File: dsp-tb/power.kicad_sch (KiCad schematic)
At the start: 16 parts, among them J1 Conn_01x03, U2 TLV76733QWDRBxQ1

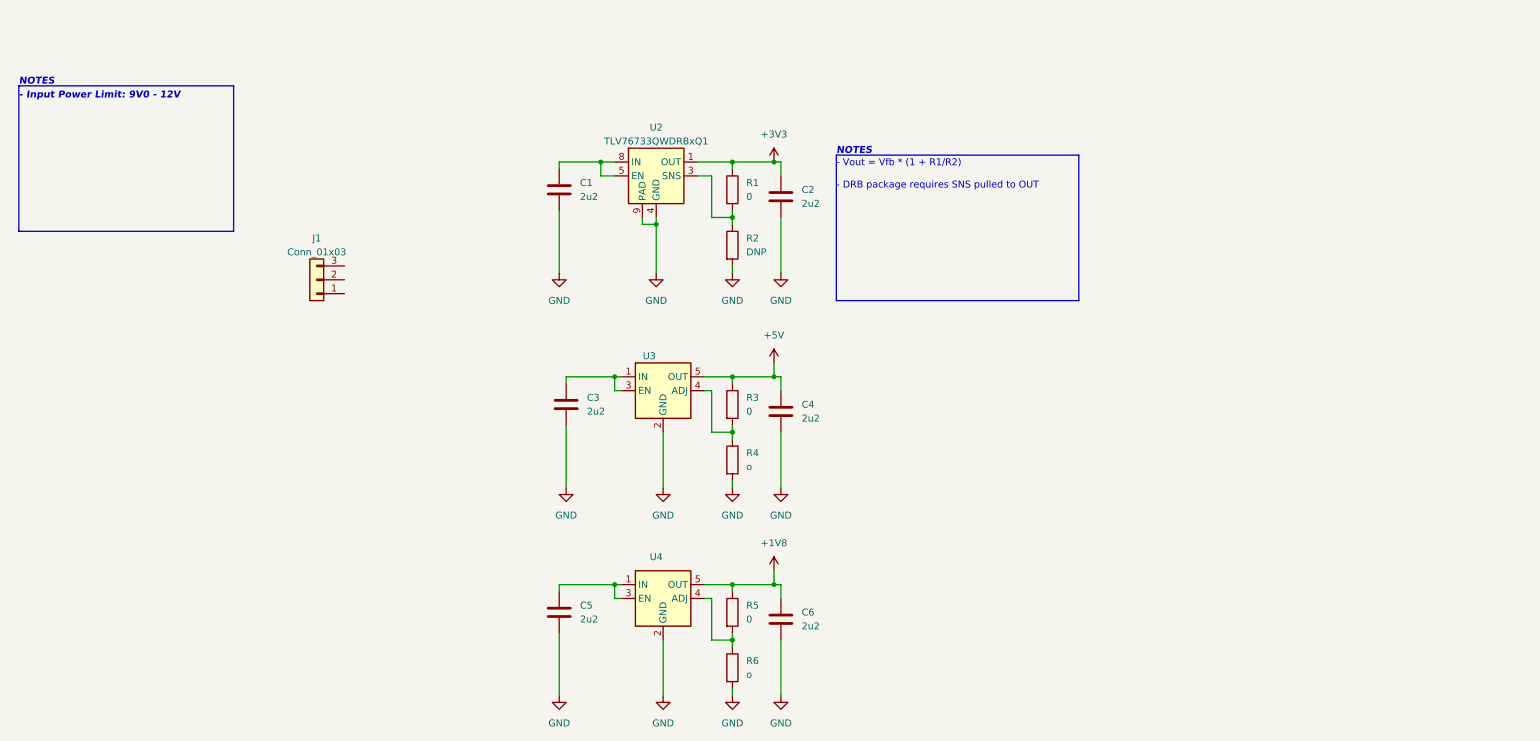
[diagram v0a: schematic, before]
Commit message: dsp-tb: start to include external components for mcu
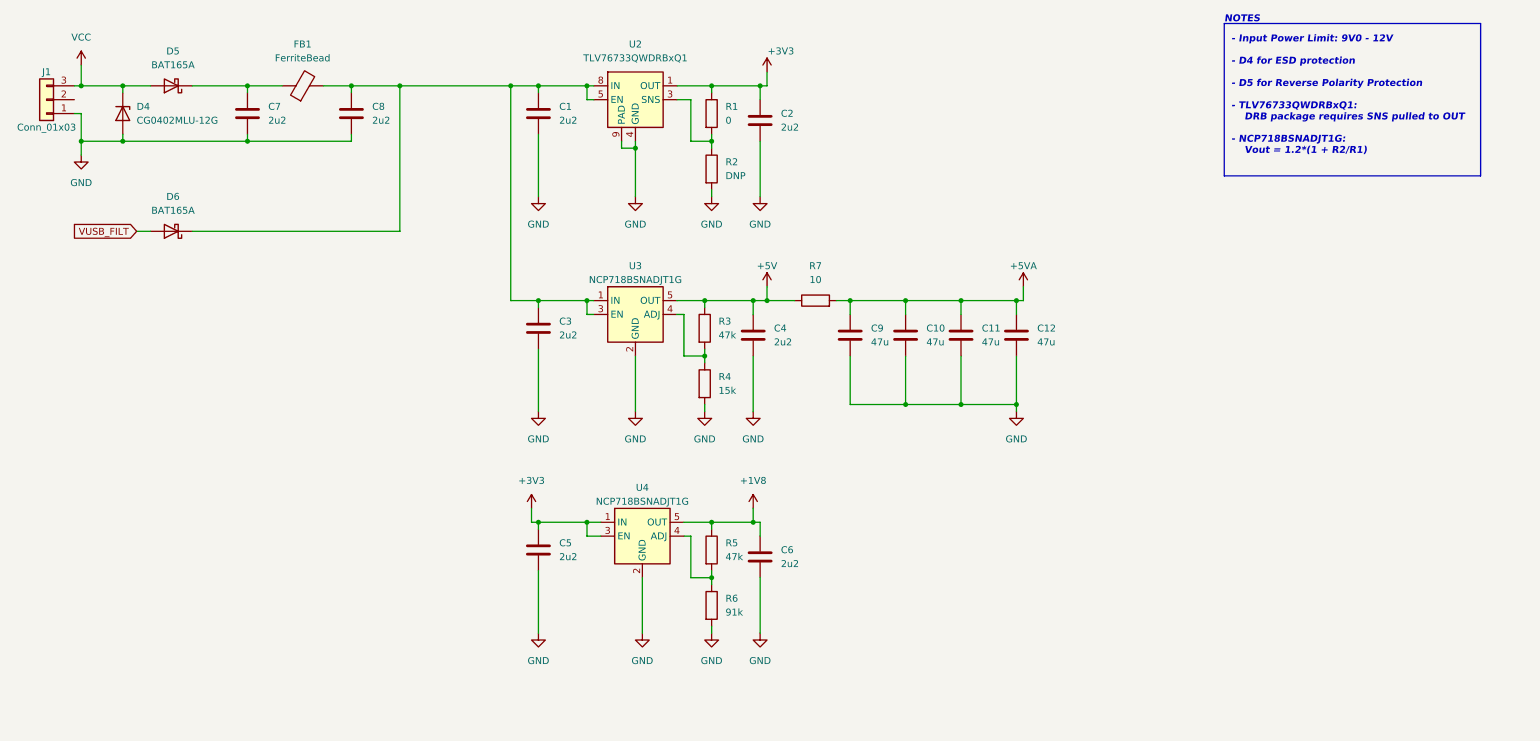
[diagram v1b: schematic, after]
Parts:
- added C10, C11, C12, C9: 47u, Capacitor_SMD:C_0402_1005Metric, symbol Device:C
- added C7, C8: 2u2, Capacitor_SMD:C_0402_1005Metric, symbol Device:C
- added D4: CG0402MLU-12G, Diode_SMD:D_0402_1005Metric, symbol Device:D_Zener
- added D5, D6: BAT165A, Diode_SMD:D_SOD-323_HandSoldering, symbol Device:D_Schottky
- added FB1: FerriteBead, Inductor_SMD:L_0402_1005Metric, symbol Device:FerriteBead
- added R7: 10, Resistor_SMD:R_0402_1005Metric, symbol Device:R
- J1: footprint (none) -> Connector_Molex:Molex_PicoBlade_53048-0310_1x03_P1.25mm_Horizontal
- R3, R5: value 0 -> 47k
- R4: value o -> 15k
- R6: value o -> 91k
- U3, U4: value ~ -> NCP718BSNADJT1G
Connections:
- net +3V3: now also C5.1, U4.1 (IN), U4.3 (EN)
- net +5V: now also R7.1
- net GND: now also J1.1 (Pin_1), C10.2, C11.2, C12.2, C7.2, C8.2, C9.2, D4.2 (A)
- net at C1.1, U2.5 (EN), U2.8 (IN): now also C3.1, U3.1 (IN), U3.3 (EN), C8.1, D6.1 (K), FB1.2
- net VCC: now reaches J1.3 (Pin_3)
- net VCC: now also D4.1 (K), D5.2 (A)
- new net: C7.1, D5.1 (K), FB1.1
- new net +5VA: C10.1, C11.1, C12.1, C9.1, R7.2
- new net VUSB_FILT: D6.2 (A)
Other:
- note added: "- Input Power Limit: 9V0 - 12V - D4 for ESD protection - D5 for Reverse Polarity Protection - TLV76733QWDRBxQ1: DRB package requires SNS pulled to OUT - NCP718BSNADJT1G: Vout = 1.2*(1 + R2/R1)"
- note removed: "- Input Power Limit: 9V0 - 12V"
- note removed: "- Vout = Vfb * (1 + R1/R2) - DRB package requires SNS pulled to OUT"
- moved on the sheet: C1, C2, C3, C4, C5, C6, J1, R1, R2, R3, R4, R5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

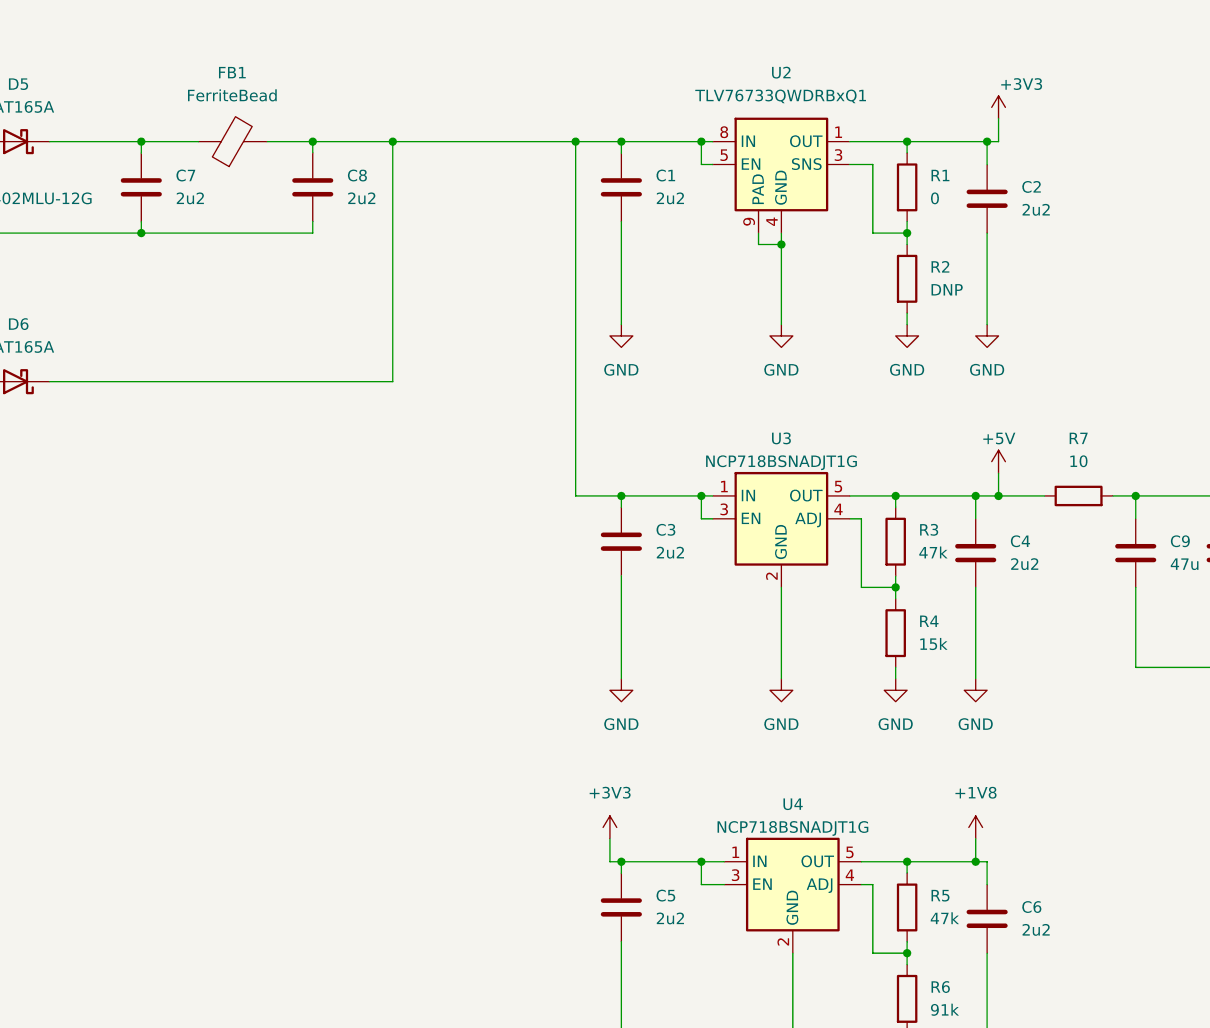
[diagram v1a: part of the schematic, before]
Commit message: dsp: boot0 and reset switches
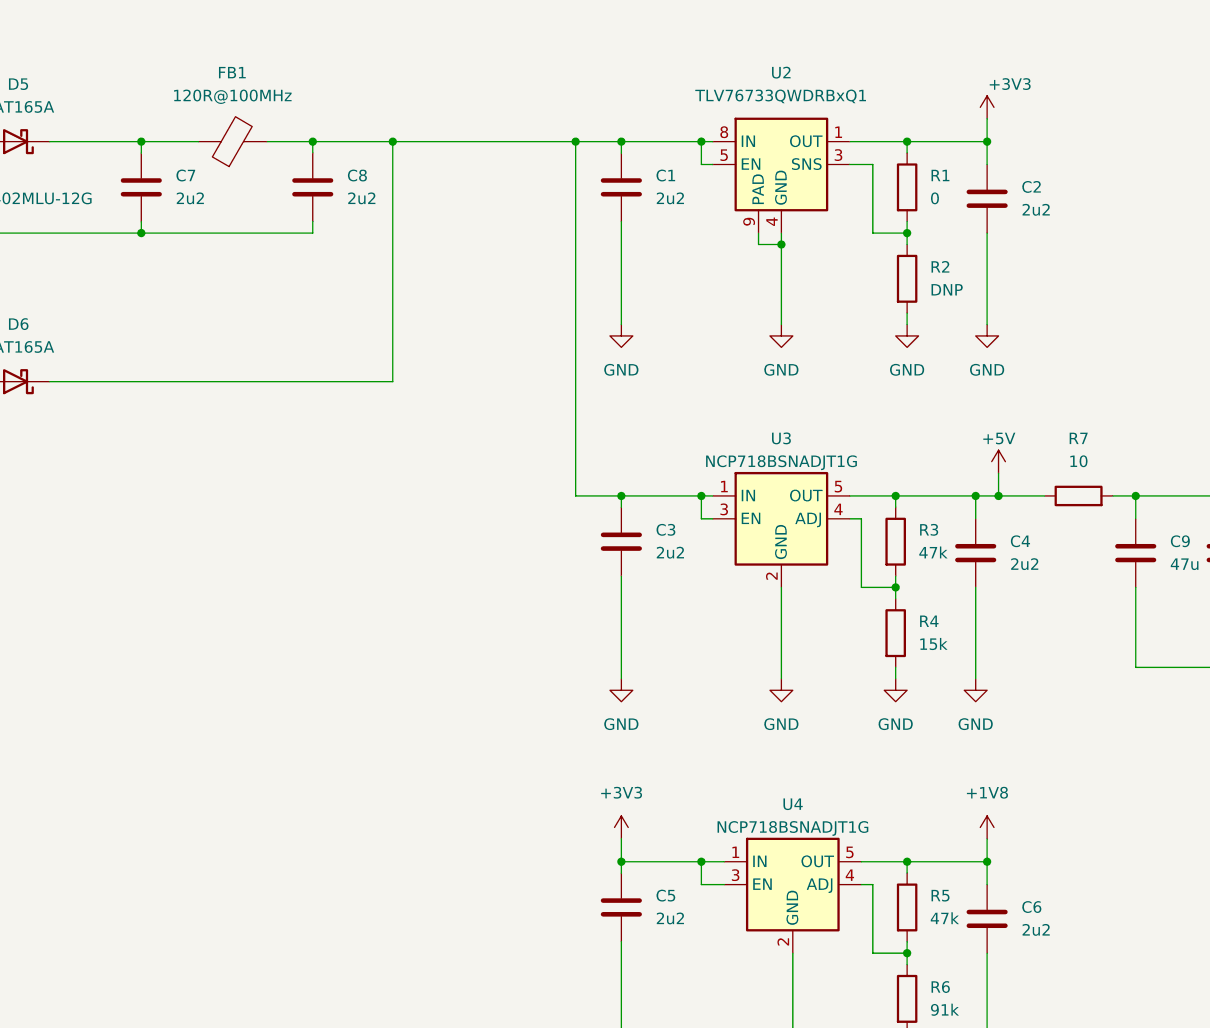
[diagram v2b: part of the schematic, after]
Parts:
- FB1: value FerriteBead -> 120R@100MHz
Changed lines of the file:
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@@
   (junction (at 142.24 36.83) (diameter 0) (color 0 0 0 0)
   )
-  (junction (at 149.86 106.68) (diameter 0) (color 0 0 0 0)
-  )
   (junction (at 142.24 26.67) (diameter 0) (color 0 0 0 0)
   )
@@
   (junction (at 119.38 26.67) (diameter 0) (color 0 0 0 0)
   )
+  (junction (at 151.13 106.68) (diameter 0) (color 0 0 0 0)
+  )
   (wire (pts (xy 34.29 26.67) (xy 39.37 26.67))
     (stroke (width 0) (type default))
@@
     (stroke (width 0) (type default))
   )
-  (wire (pts (xy 149.86 106.68) (xy 151.13 106.68))
-    (stroke (width 0) (type default))
-  )
   (wire (pts (xy 151.13 36.83) (xy 151.13 46.99))
     (stroke (width 0) (type default))
@@
     (stroke (width 0) (type default))
   )
-  (wire (pts (xy 109.22 104.14) (xy 109.22 106.68))
+  (wire (pts (xy 110.49 104.14) (xy 110.49 106.68))
     (stroke (width 0) (type default))
   )
@@
     (stroke (width 0) (type default))
   )
-  (wire (pts (xy 142.24 106.68) (xy 149.86 106.68))
+  (wire (pts (xy 142.24 106.68) (xy 151.13 106.68))
     (stroke (width 0) (type default))
   )
@@
     (stroke (width 0) (type default))
   )
-  (wire (pts (xy 109.22 106.68) (xy 110.49 106.68))
-    (stroke (width 0) (type default))
-  )
   (wire (pts (xy 140.97 67.31) (xy 140.97 66.04))
     (stroke (width 0) (type default))
@@
     (stroke (width 0) (type default))
   )
-  (wire (pts (xy 152.4 26.67) (xy 151.13 26.67))
-    (stroke (width 0) (type default))
-  )
   (wire (pts (xy 57.15 26.67) (xy 63.5 26.67))
     (stroke (width 0) (type default))
@@
     (stroke (width 0) (type default))
   )
-  (wire (pts (xy 149.86 104.14) (xy 149.86 106.68))
+  (wire (pts (xy 151.13 104.14) (xy 151.13 106.68))
     (stroke (width 0) (type default))
   )
@@
     (stroke (width 0) (type default))
   )
-  (wire (pts (xy 152.4 24.13) (xy 152.4 26.67))
+  (wire (pts (xy 151.13 24.13) (xy 151.13 26.67))
     (stroke (width 0) (type default))
   )
@@
       (effects (font (size 1.27 1.27)))
     )
-    (property "Value" "FerriteBead" (at 67.2592 21.59 90)
+    (property "Value" "120R@100MHz" (at 67.2592 21.59 90)
       (effects (font (size 1.27 1.27)))
     )
@@
     )
   )
-  (symbol (lib_id "power:+3V3") (at 109.22 104.14 0) (unit 1)
-    (in_bom yes) (on_board yes) (dnp no) (fields_autoplaced)
-    (property "Reference" "#PWR018" (at 109.22 107.95 0)
-      (effects (font (size 1.27 1.27)) hide)
-    )
-    (property "Value" "+3V3" (at 109.22 99.06 0)
-      (effects (font (size 1.27 1.27)))
-    )
-    (property "Footprint" "" (at 109.22 104.14 0)
-      (effects (font (size 1.27 1.27)) hide)
-    )
-    (property "Datasheet" "" (at 109.22 104.14 0)
+  (symbol (lib_id "power:+3V3") (at 110.49 104.14 0) (unit 1)
+    (in_bom yes) (on_board yes) (dnp no) (fields_autoplaced)
+    (property "Reference" "#PWR018" (at 110.49 107.95 0)
+      (effects (font (size 1.27 1.27)) hide)
+    )
+    (property "Value" "+3V3" (at 110.49 99.06 0)
+      (effects (font (size 1.27 1.27)))
+    )
+    (property "Footprint" "" (at 110.49 104.14 0)
+      (effects (font (size 1.27 1.27)) hide)
+    )
+    (property "Datasheet" "" (at 110.49 104.14 0)
       (effects (font (size 1.27 1.27)) hide)
     )
@@
     )
   )
-  (symbol (lib_id "power:+1V8") (at 149.86 104.14 0) (unit 1)
-    (in_bom yes) (on_board yes) (dnp no) (fields_autoplaced)
-    (property "Reference" "#PWR010" (at 149.86 107.95 0)
-      (effects (font (size 1.27 1.27)) hide)
-    )
-    (property "Value" "+1V8" (at 149.86 99.06 0)
-      (effects (font (size 1.27 1.27)))
-    )
-    (property "Footprint" "" (at 149.86 104.14 0)
-      (effects (font (size 1.27 1.27)) hide)
-    )
-    (property "Datasheet" "" (at 149.86 104.14 0)
+  (symbol (lib_id "power:+1V8") (at 151.13 104.14 0) (unit 1)
+    (in_bom yes) (on_board yes) (dnp no) (fields_autoplaced)
+    (property "Reference" "#PWR010" (at 151.13 107.95 0)
+      (effects (font (size 1.27 1.27)) hide)
+    )
+    (property "Value" "+1V8" (at 151.13 99.06 0)
+      (effects (font (size 1.27 1.27)))
+    )
+    (property "Footprint" "" (at 151.13 104.14 0)
+      (effects (font (size 1.27 1.27)) hide)
+    )
+    (property "Datasheet" "" (at 151.13 104.14 0)
       (effects (font (size 1.27 1.27)) hide)
     )
@@
     )
   )
-  (symbol (lib_id "power:+3V3") (at 152.4 24.13 0) (unit 1)
+  (symbol (lib_id "power:+3V3") (at 151.13 24.13 0) (unit 1)
     (in_bom yes) (on_board yes) (dnp no)
-    (property "Reference" "#PWR08" (at 152.4 27.94 0)
-      (effects (font (size 1.27 1.27)) hide)
-    )
-    (property "Value" "+3V3" (at 154.94 20.32 0)
-      (effects (font (size 1.27 1.27)))
-    )
-    (property "Footprint" "" (at 152.4 24.13 0)
-      (effects (font (size 1.27 1.27)) hide)
-    )
-    (property "Datasheet" "" (at 152.4 24.13 0)
-      (effects (font (size 1.27 1.27)) hide)
-    )
+    (property "Reference" "#PWR08" (at 151.13 27.94 0)
+      (effects (font (size 1.27 1.27)) hide)
+    )
+    (property "Value" "+3V3" (at 153.67 20.32 0)
+      (effects (font (size 1.27 1.27)))
+    )
+    (property "Footprint" "" (at 151.13 24.13 0)
+      (effects (font (size 1.27 1.27)) hide)
+    )
+    (property "Datasheet" "" (at 151.13 24.13 0)
+      (effects (font (size 1.27 1.27)) hide)
+    )

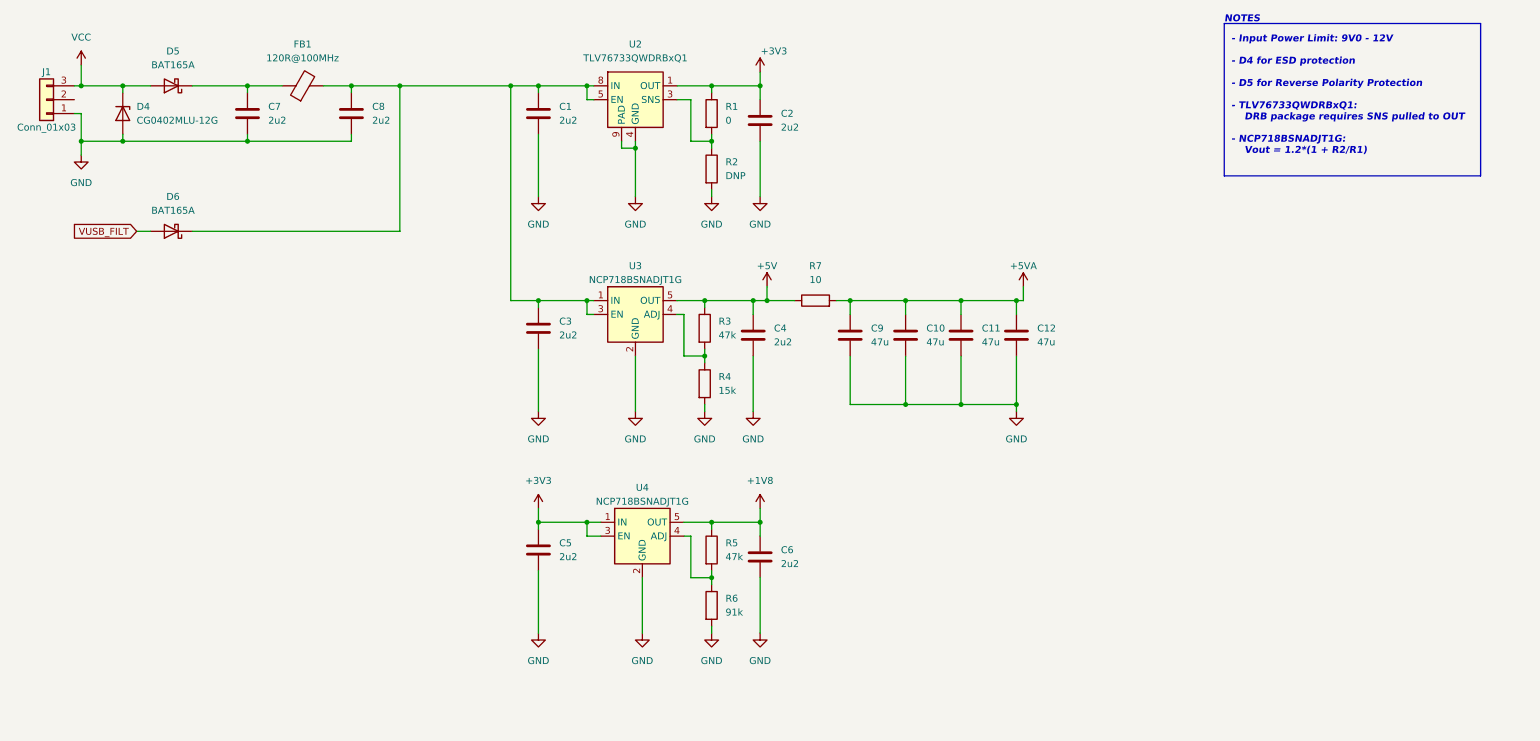
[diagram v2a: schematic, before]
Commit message: dsp-tb: finish schematic drawings
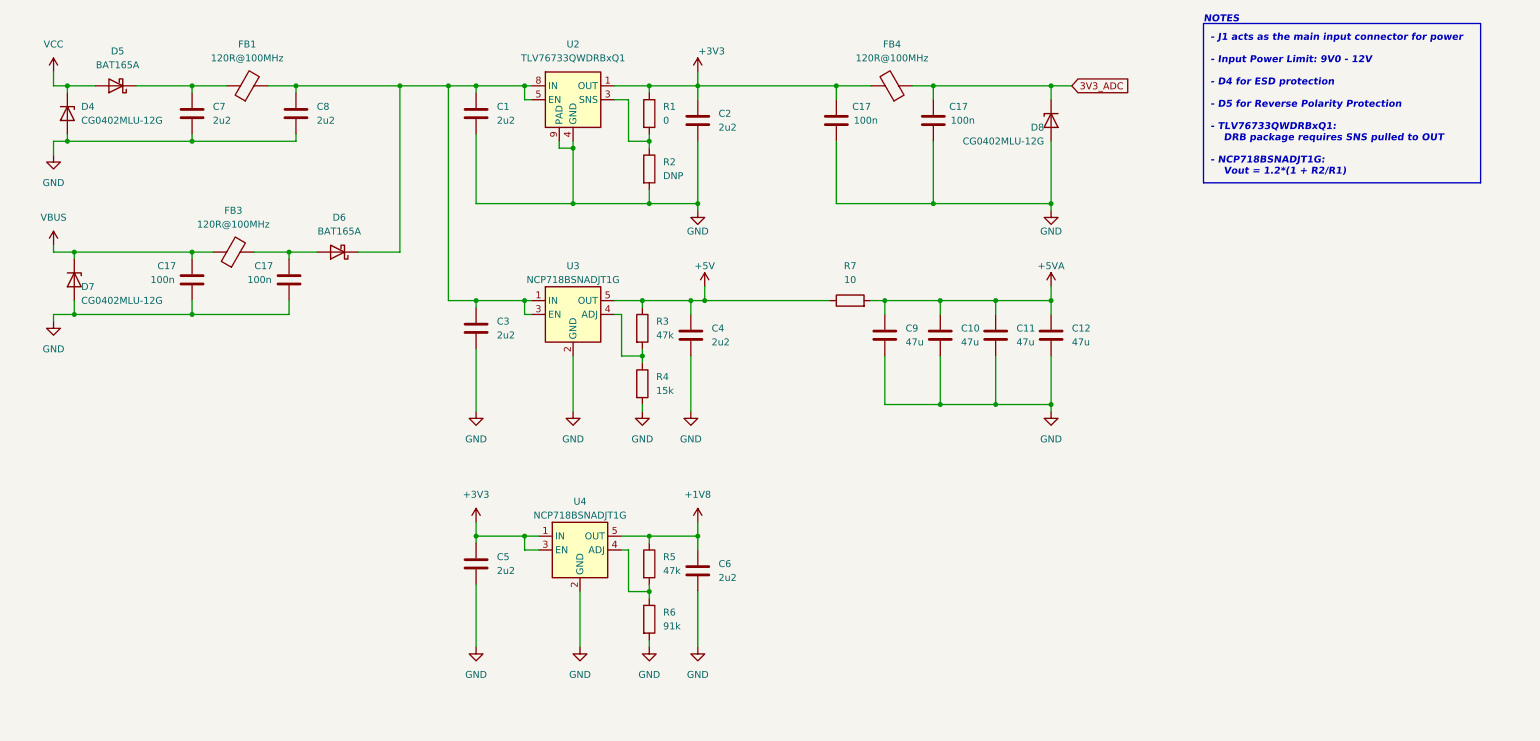
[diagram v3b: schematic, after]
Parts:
- removed J1: Conn_01x03, Connector_Molex:Molex_PicoBlade_53048-0310_1x03_P1.25mm_Horizontal, symbol Connector_Generic:Conn_01x03
- added C17 (x4): 100n, Capacitor_SMD:C_0402_1005Metric, symbol Device:C
- added D7, D8: CG0402MLU-12G, Diode_SMD:D_0402_1005Metric, symbol Device:D_Zener
- added FB3, FB4: 120R@100MHz, Inductor_SMD:L_0402_1005Metric, symbol Device:FerriteBead
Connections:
- net +3V3: now also C17.1, FB4.2
- net GND: now also C17.2, C17.2, C17.2, C17.2, D7.2 (A), D8.2 (A)
- net VUSB_FILT: no longer names the net of D6.2 (A)
- net VUSB_FILT: now also C17.1, FB3.2
- new net 3V3_ADC: C17.1, D8.1 (K), FB4.1
- new net VBUS: C17.1, D7.1 (K), FB3.1
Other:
- note added: "- J1 acts as the main input connector for power - Input Power Limit: 9V0 - 12V - D4 for ESD protection - D5 for Reverse Polarity Protection - TLV76733QWDRBxQ1: DRB package requires SNS pulled to OUT - NCP718BSNADJT1G: Vout = 1.2*(1 + R2/R1)"
- note removed: "- Input Power Limit: 9V0 - 12V - D4 for ESD protection - D5 for Reverse Polarity Protection - TLV76733QWDRBxQ1: DRB package requires SNS pulled to OUT - NCP718BSNADJT1G: Vout = 1.2*(1 + R2/R1)"
- moved on the sheet: C1, C10, C11, C12, C2, C3, C4, C5, C6, C7, C8, C9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
